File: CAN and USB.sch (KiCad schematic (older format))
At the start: 24 parts, among them U4 AMS1117-3.3, U5 L78L05_SOT89, U6 TJA1042T-3, U7 STM32F072C8, Y1 8MHz

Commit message: Good-enough for first PCB attempt.
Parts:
- removed C40, C41: 18pF, Capacitor_SMD:C_0603_1608Metric, symbol Device:C_Small
- removed D28: LED_RGB, symbol Device:LED_RGB
- removed R72: 0R, Resistor_SMD:R_0603_1608Metric, symbol bldc-BMS-rescue:R_Small
- removed Y1: 8MHz, Oscillator:Oscillator_SMD_Abracon_ASE-4Pin_3.2x2.5mm, symbol Device:Crystal_Small
- added C11: 470nF, Capacitor_SMD:C_0603_1608Metric, symbol Device:C_Small
- added C12, C16: 15pF, Capacitor_SMD:C_0603_1608Metric, symbol Device:C_Small
- added D13: BLUE, LED_SMD:LED_0603_1608Metric_Pad1.05x0.95mm_HandSolder, symbol Device:LED_ALT
- added D8: RED, LED_SMD:LED_0603_1608Metric_Pad1.05x0.95mm_HandSolder, symbol Device:LED_ALT
- added D9: GREEN, LED_SMD:LED_0603_1608Metric_Pad1.05x0.95mm_HandSolder, symbol Device:LED_ALT
- added JP2: Jumper_NO, Jumper:SolderJumper-2_P1.3mm_Open_TrianglePad1.0x1.5mm, symbol Device:Jumper_NO_Small
- added JP3: Jumper_NC_Small, Jumper:SolderJumper-2_P1.3mm_Bridged_RoundedPad1.0x1.5mm, symbol Device:Jumper_NC_Small
- added Y1: 8MHz, Crystal:Crystal_SMD_5032-4Pin_5.0x3.2mm, symbol Device:Crystal_GND24
- C32, C33: Description (none) -> CAP CER 2.2UF 16V X5R 0603; Digikey PN (none) -> 1276-1040-1-ND
- C34: Description (none) -> CAP TANT POLY 100UF 6.3V 1206; Digikey PN (none) -> 478-9563-1-ND
- C35, C37, C38, C39: value 2.2uF -> 0.1uF; Description (none) -> CAP CER 0.1UF 25V X7R 0603; Digikey PN (none) -> 311-1341-1-ND
- C36: Description (none) -> CAP CER 0.1UF 25V X7R 0603; Digikey PN (none) -> 311-1341-1-ND
- D29: footprint (none) -> bldc-BMS:D_SOT-23_TVS; Description (none) -> TRANSIENT VOLTAGE SUPPRESSOR DIO; Digikey PN (none) -> RESD1CANFHT116CT-ND
- R75: value 220R -> 1k
- R76, R77: value 22 -> 22R
- R78: value 120 -> 120R
- U4: value AMS1117-3.3 -> MIC5219-3.3; footprint Package_TO_SOT_SMD:SOT-223-3_TabPin2 -> bldc-BMS:SOT-23-5; symbol Regulator_Linear:AMS1117-3.3 -> bldc-BMS:MIC5219-3.3; Description (none) -> IC REG LINEAR 3.3V 500MA SOT23-5; Digikey PN (none) -> 576-1281-1-ND
- U5: value L78L05_SOT89 -> MIC5239-5.0; footprint Package_TO_SOT_SMD:SOT-89-3 -> Package_TO_SOT_SMD:SOT-223; symbol Regulator_Linear:L78L05_SOT89 -> bldc-BMS:MIC5239-5.0; Description (none) -> IC REG LINEAR 5V 500MA SOT223; Digikey PN (none) -> 576-2397-1-ND
- U6: Description (none) -> IC CAN TRANSEIVER HS 8SOIC; Digikey PN (none) -> 568-8678-1-ND
- U7: footprint Package_QFP:LQFP-48-1EP_7x7mm_P0.5mm_EP3.6x3.6mm -> Package_QFP:LQFP-48_7x7mm_P0.5mm; Description (none) -> IC MCU 32BIT 64KB FLASH 48LQFP; Digikey PN (none) -> 497-17359-1-ND
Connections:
- net labels added: ~ENABLE
- wire segments 132 -> 149
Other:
- note added: "OPTIONAL\nCAN TERM"
- note removed: "CAN TERM"
- note removed: "Populate 0R for Battery Monitor 3.3V supply. \nDon't populate 3.3V regulator."
- moved on the sheet: C32, C34

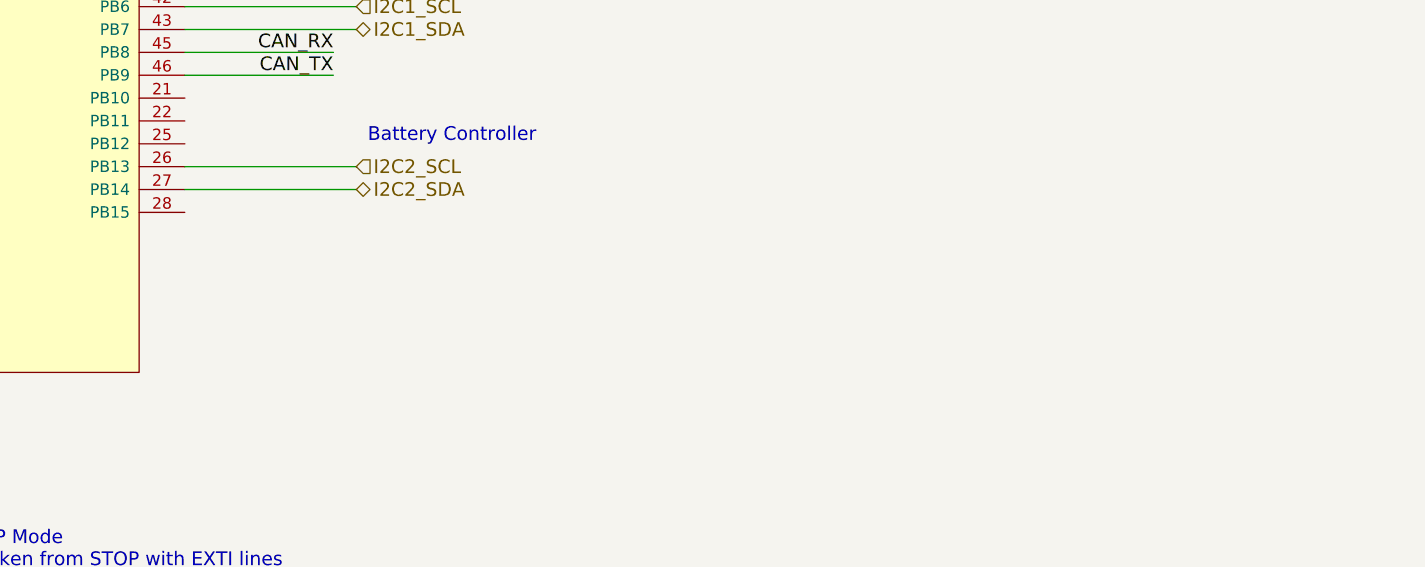
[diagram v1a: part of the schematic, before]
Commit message: first PCB spin for testing
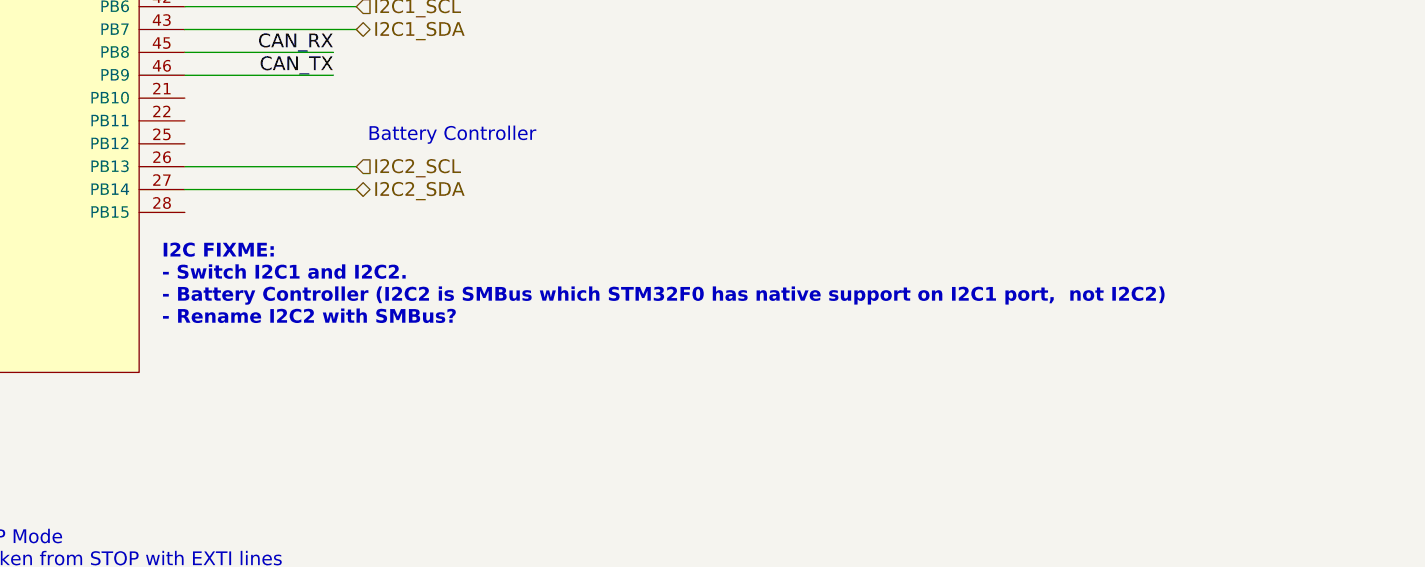
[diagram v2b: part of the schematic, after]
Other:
- note added: "I2C FIXME:\n- Switch I2C1 and I2C2. \n- Battery Controller (I2C2 is SMBus which STM32F0 has native support on I2C1 port, not I2C2)\n- Rename I2C2 with SMBus?"
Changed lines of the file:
@@
 EESchema Schematic File Version 4
 LIBS:bldc-BMS-cache
-EELAYER 29 0
+EELAYER 30 0
 EELAYER END
 $Descr A4 11693 8268
@@
 $EndComp
 Connection ~ 8250 2250
+Text Notes 6500 4700 0    60   ~ 12
+I2C FIXME:\n- Switch I2C1 and I2C2. \n- Battery Controller (I2C2 is SMBus which STM32F0 has native support on I2C1 port,  not I2C2)\n- Rename I2C2 with SMBus?
 $EndSCHEMATC
